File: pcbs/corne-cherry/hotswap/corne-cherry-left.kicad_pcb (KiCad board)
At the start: 2 copper layers, 160 x 109.4 mm, 47 parts, among them J2 ST-0277D00-052-142, J3 Conn_01x04, SW1 SW_Push, SW10 SW_Push, SW11 SW_Push, SW12 SW_Push, SW13 SW_Push, SW14 SW_Push, SW15 SW_Push, SW16 SW_Push, SW17 SW_Push, SW18 SW_Push, SW19 SW_Push, SW2 SW_Push, SW20 SW_Push, SW21 SW_Push, SW3 SW_Push, SW4 SW_Push, SW5 SW_Push, SW6 SW_Push, SW7 SW_Push, SW8 SW_Push, SW9 SW_Push, U5 rp2040

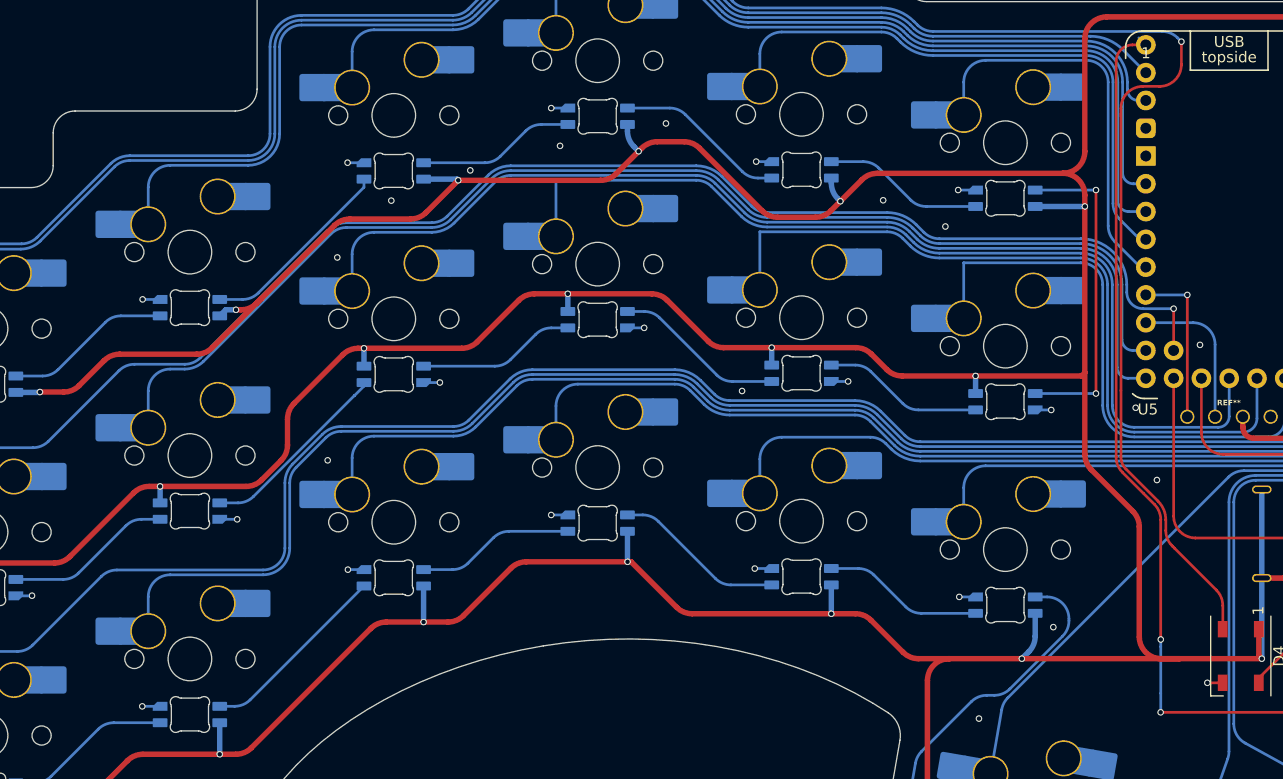
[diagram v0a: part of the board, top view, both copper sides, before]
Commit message: split into left and right
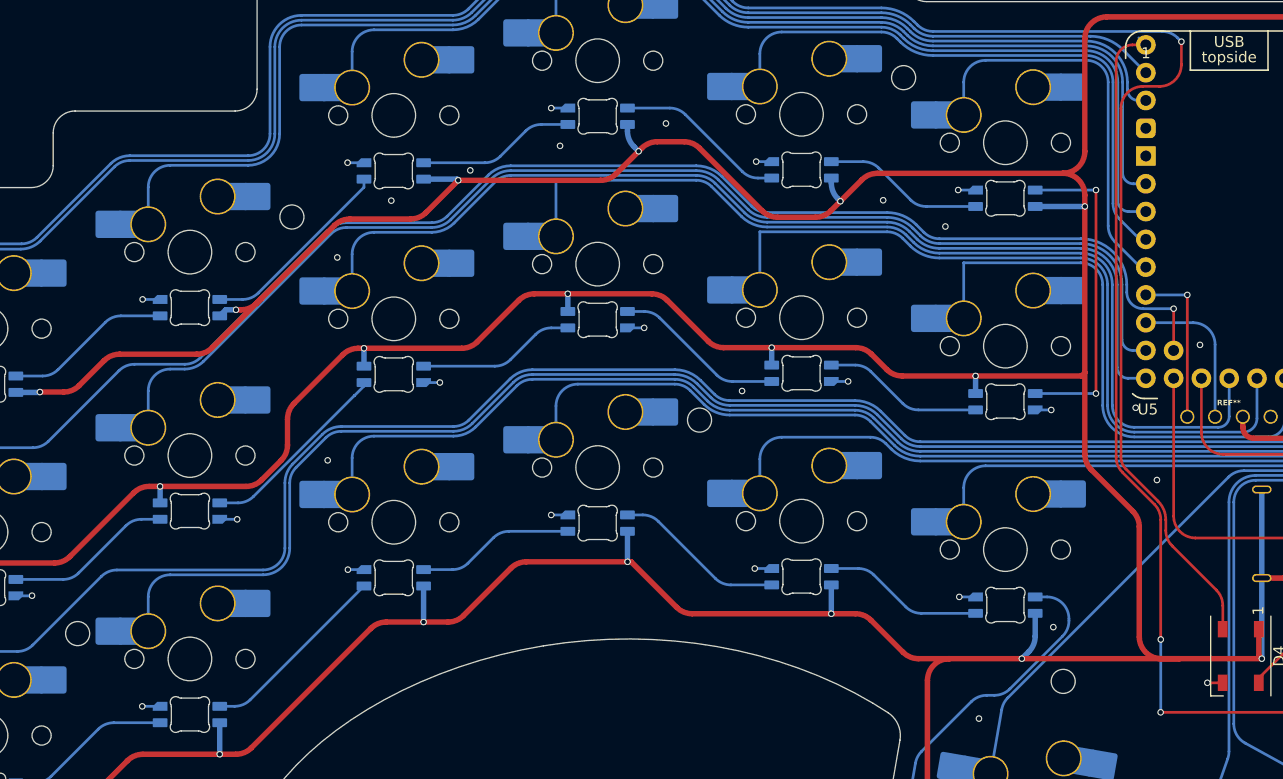
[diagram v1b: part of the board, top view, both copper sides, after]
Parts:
- added REF**: MountingHole_2.2mm_M2, MountingHole:MountingHole_2.2mm_M2, F.Cu at (149.7, 116.3)
- added REF**: MountingHole_2.2mm_M2, MountingHole:MountingHole_2.2mm_M2, F.Cu at (164.3, 171.5)
- added REF**: MountingHole_2.2mm_M2, MountingHole:MountingHole_2.2mm_M2, F.Cu at (93.8, 129.1)
- added REF**: MountingHole_2.2mm_M2, MountingHole:MountingHole_2.2mm_M2, F.Cu at (131.1, 147.6)
- added REF**: MountingHole_2.2mm_M2, MountingHole:MountingHole_2.2mm_M2, F.Cu at (74.2, 167.1)

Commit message: add skqg
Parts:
- removed J2: ST-0277D00-052-142, kbd_local:ST-0277D00-052-142
- added REF**: SW_SPST_SKQG_WithStem, PCM_marbastlib-various:SW_SPST_SKQG_WithStem, B.Cu at (179.4, 120.7)
- added TRRS: PJ-320A, PJ-320A_Library:PJ-320A, F.Cu at (195.7, 160.2)
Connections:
- U5 pad rst: (no net) -> rst
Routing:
- net rst: track 0.00 -> 11.5 mm
- net GND: track 34.7 -> 45.9 mm
- net /left/RX: track 19.2 -> 25.1 mm
- net +5V: track 642.2 -> 638.4 mm, vias 22 -> 23
- net /left/TX: track 32.6 -> 31.6 mm, vias 0 -> 2
